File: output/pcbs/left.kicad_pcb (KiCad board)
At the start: 2 copper layers, 115.8 x 102 mm, 69 parts

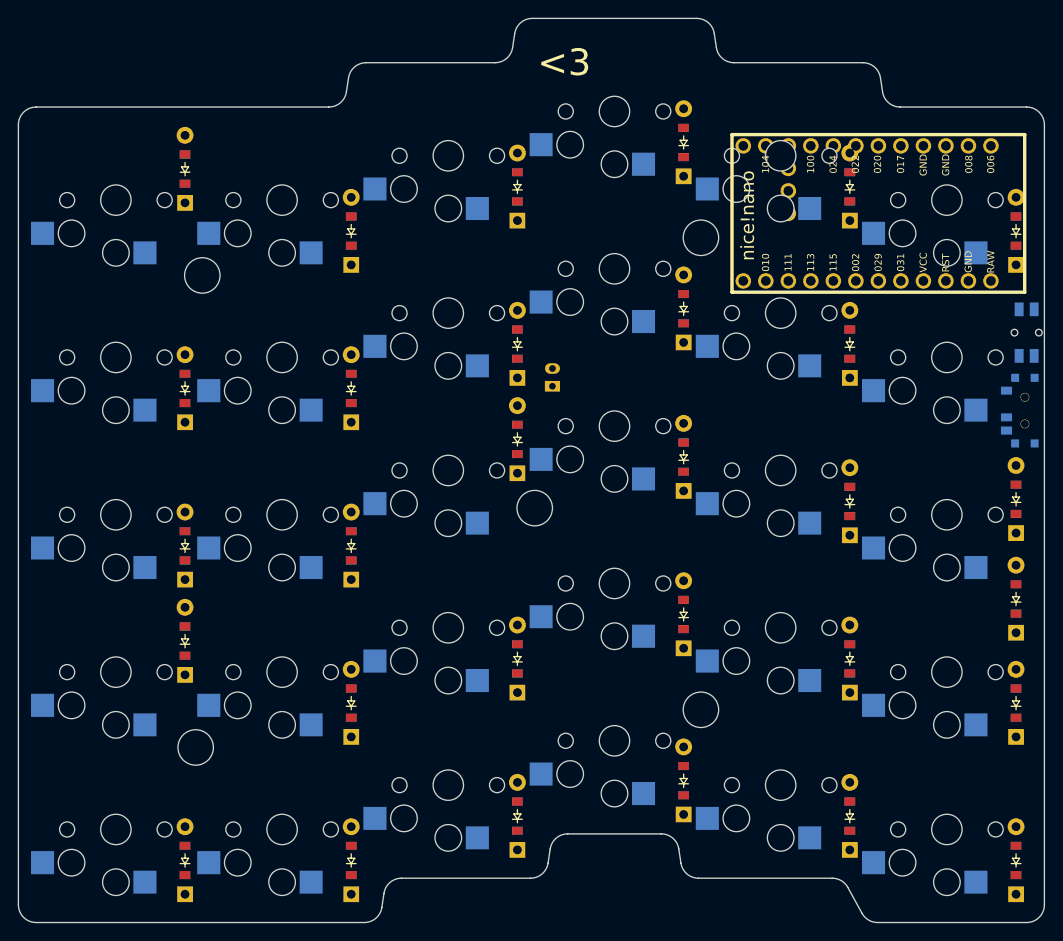
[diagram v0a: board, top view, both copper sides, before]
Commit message: changed nice!nano position
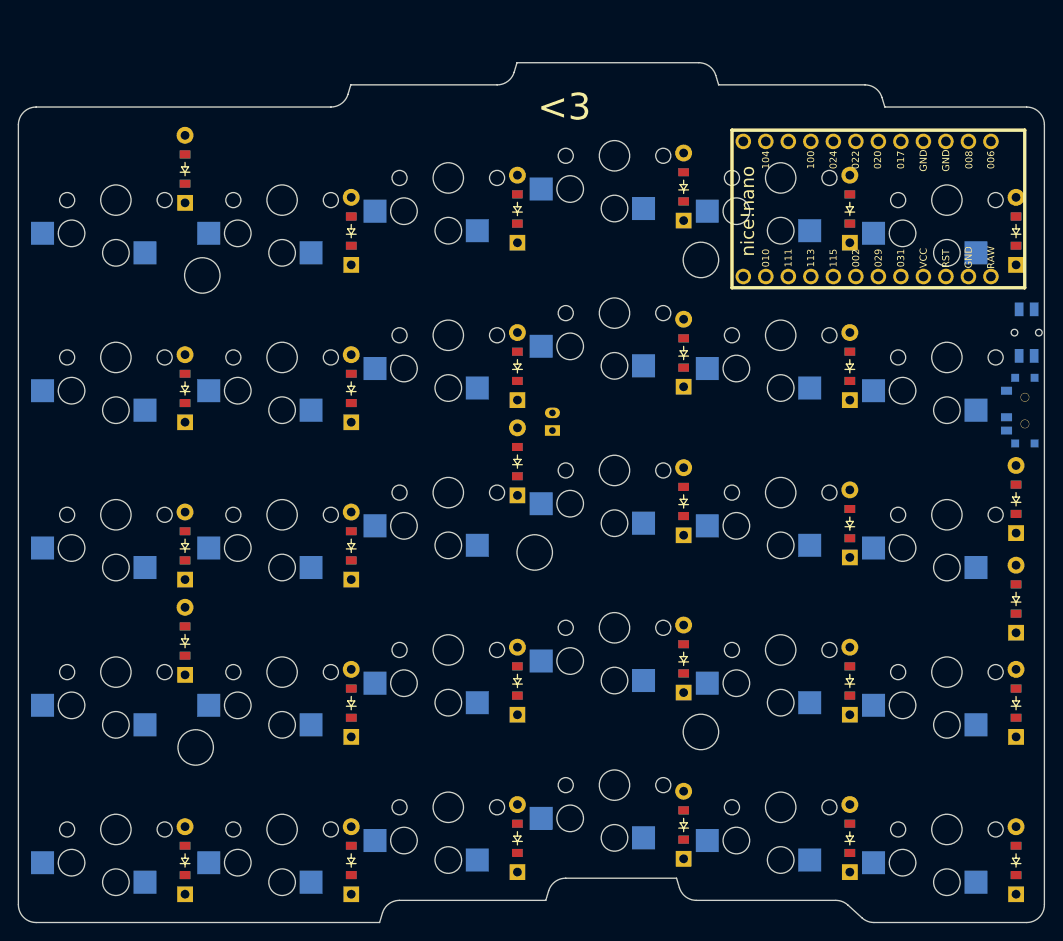
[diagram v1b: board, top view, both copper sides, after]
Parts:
- removed the ? at (166.0, 136.5)
- removed the ? at (166.0, 83.2)
- removed the ? at (147.2, 113.8)
- added ?: , HOLE_M2_TH, F.Cu at (166.0, 139.0)
- added ?: , HOLE_M2_TH, F.Cu at (166.0, 85.8)
- added ?: , HOLE_M2_TH, F.Cu at (147.2, 118.8)
- moved D13 5.00 mm to (164.1, 130.8)
- moved D14 5.00 mm to (164.1, 113.0)
- moved D15 5.00 mm to (164.1, 77.5)
- moved D29 5.00 mm to (164.1, 149.5)
- moved D30 5.00 mm to (164.1, 96.2)
- moved JST1 5.00 mm to (149.2, 104.0)
- moved S16 5.00 mm to (156.2, 145.0)
- moved S17 5.00 mm to (156.2, 127.2)
- moved S18 5.00 mm to (156.2, 109.5)
- moved S19 5.00 mm to (156.2, 91.8)
- moved S20 5.00 mm to (156.2, 74.0)
- moved D10 2.50 mm to (145.3, 133.2)
- moved D11 2.50 mm to (145.3, 97.8)
- moved D12 2.50 mm to (145.3, 80.0)
- moved D16 2.50 mm to (182.8, 151.0)
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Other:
- board size 115.8 x 102 mm -> 115.8 x 97 mm

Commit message: added readme
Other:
- board text added: "WHISPER"
- board text removed: "<3"
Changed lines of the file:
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@@
       (at 147.25 118.75 0)
       (pad "" np_thru_hole circle (at 0 0 90) (size 4.0 4.0) (drill 4.0) (layers *.Cu *.Mask F.SilkS) (clearance 0.3)))
-            (gr_text "<3" (at 147.55 68.5 0) (layer F.SilkS)
+            (gr_text "WHISPER" (at 147.55 68.5 0) (layer F.SilkS)
                 (effects (font (size 3 3) (thickness 0.4) ) (justify left))
             )
